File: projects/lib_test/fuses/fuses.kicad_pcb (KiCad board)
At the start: 2 copper layers, 80 x 60 mm, 0 parts

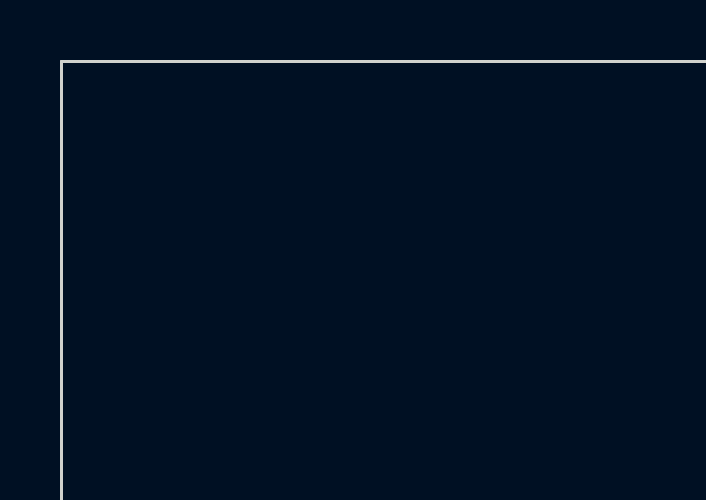
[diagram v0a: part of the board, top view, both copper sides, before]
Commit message: updated fuses test project
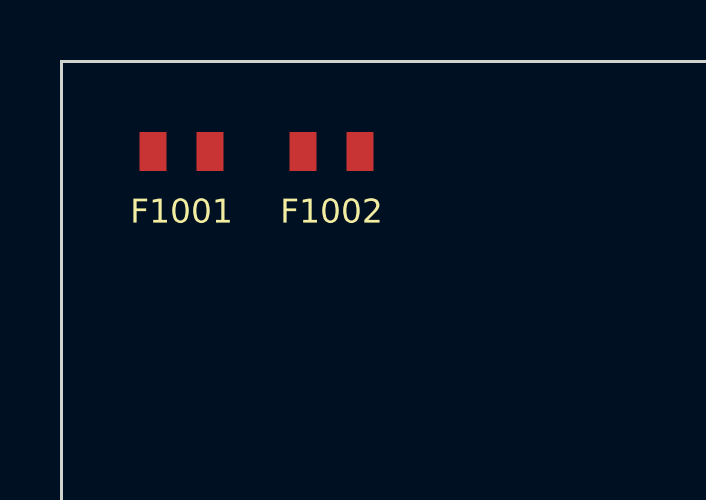
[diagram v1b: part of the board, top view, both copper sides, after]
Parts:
- added F1001: 0.1A/0.3A, lily_footprints:fuse_ptc_0805, F.Cu at (114.0, 73.0)
- added F1002: 0.35A/0.75A, lily_footprints:fuse_ptc_0805, F.Cu at (119.0, 73.0)
